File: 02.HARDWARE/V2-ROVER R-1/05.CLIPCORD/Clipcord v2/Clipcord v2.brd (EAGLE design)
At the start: 24 x 12.2 mm, 0 parts

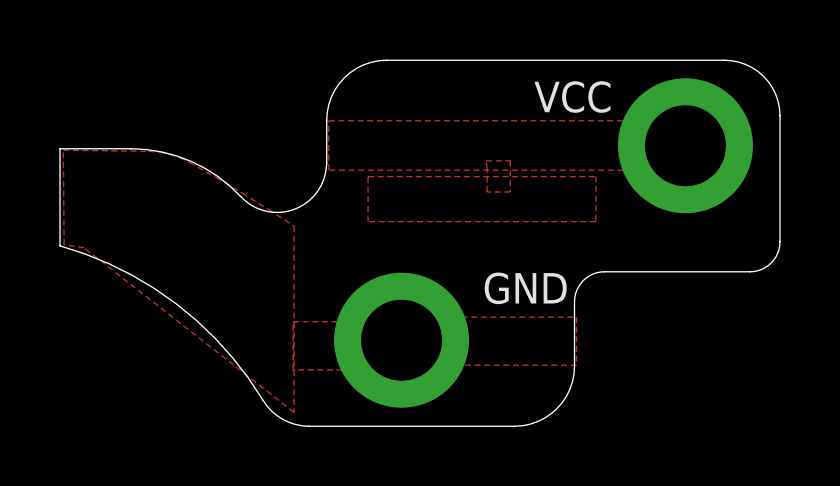
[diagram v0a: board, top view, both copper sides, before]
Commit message: Modificación de la dimension del PCB
version 2
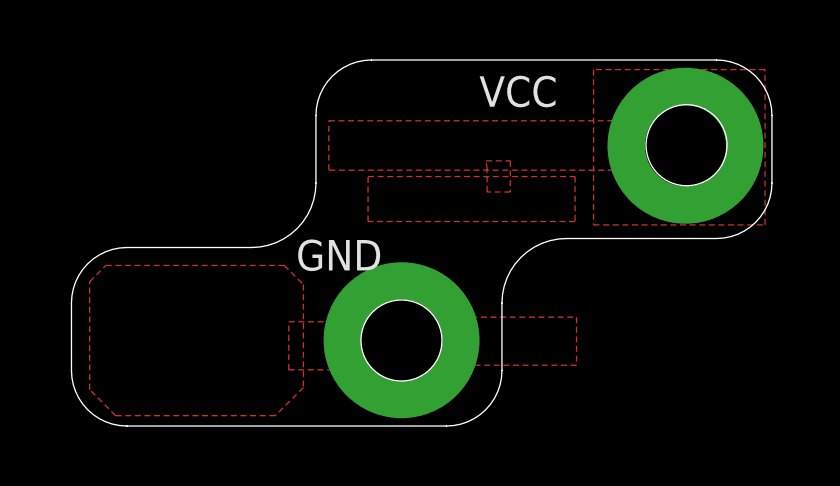
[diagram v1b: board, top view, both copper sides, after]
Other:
- board size 24 x 12.2 mm -> 23.3 x 12.2 mm
